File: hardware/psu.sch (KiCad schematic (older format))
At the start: 15 parts, among them U2 MIC5233-3.3

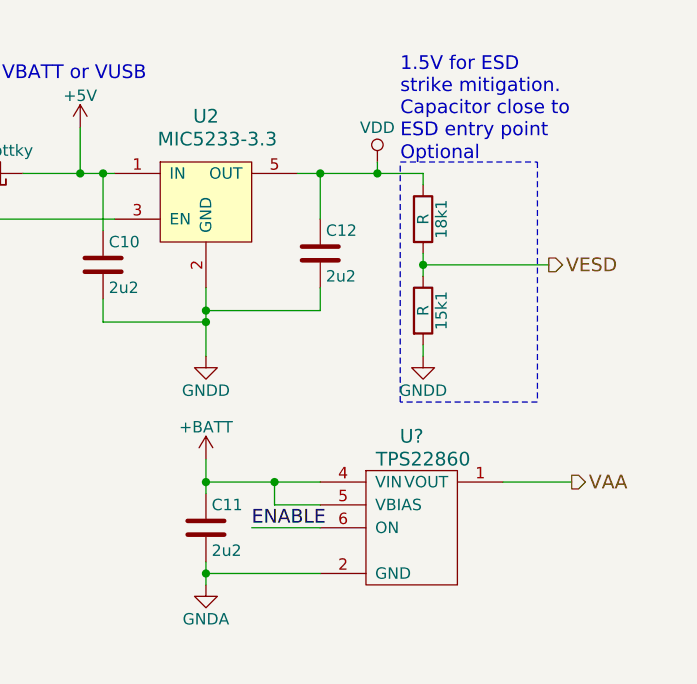
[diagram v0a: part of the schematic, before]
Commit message: Fix annotation of VESD resistors
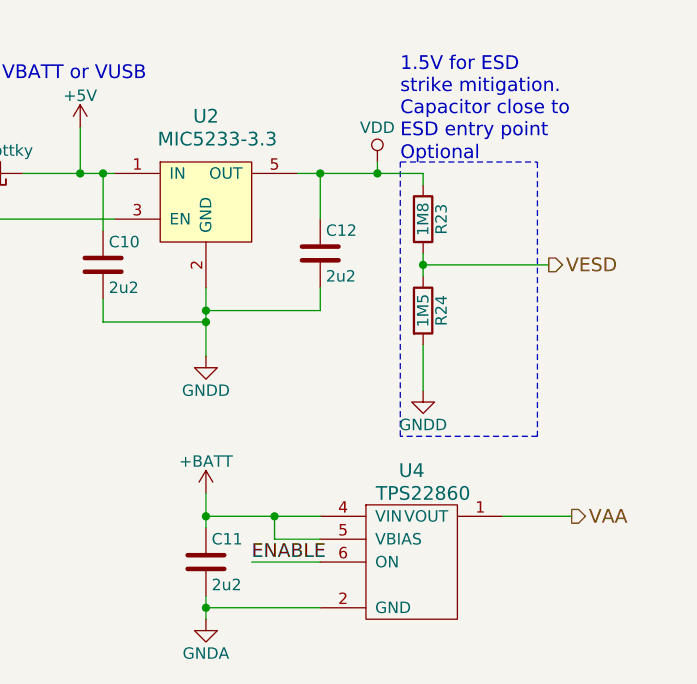
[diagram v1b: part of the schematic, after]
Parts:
- R23: renamed from 18k1; value R -> 1M8
- R24: renamed from 15k1; value R -> 1M5
- gave numbers to parts that had none: 1
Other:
- moved on the sheet: C11, U4
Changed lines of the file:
@@
 LIBS:mic5233-xx
 LIBS:bat54s
+LIBS:tps22860
 LIBS:musamasiina-cache
 EELAYER 25 0
@@
 $EndComp
 $Comp
-L GNDD #PWR025
+L GNDD #PWR27
 U 1 1 573FE50E
 P 3150 5550
-F 0 "#PWR025" H 3150 5300 50  0001 C CNN
+F 0 "#PWR27" H 3150 5300 50  0001 C CNN
 F 1 "GNDD" H 3150 5400 50  0000 C CNN
 F 2 "" H 3150 5550 50  0000 C CNN
@@
 $EndComp
 $Comp
-L +BATT #PWR026
+L +BATT #PWR25
 U 1 1 573FE50F
 P 1850 4550
-F 0 "#PWR026" H 1850 4400 50  0001 C CNN
+F 0 "#PWR25" H 1850 4400 50  0001 C CNN
 F 1 "+BATT" H 1850 4690 50  0000 C CNN
 F 2 "" H 1850 4550 50  0000 C CNN
@@
 $EndComp
 $Comp
-L VDD #PWR027
+L VDD #PWR33
 U 1 1 573FE51D
 P 3900 4700
-F 0 "#PWR027" H 3900 4550 50  0001 C CNN
+F 0 "#PWR33" H 3900 4550 50  0001 C CNN
 F 1 "VDD" H 3900 4850 50  0000 C CNN
 F 2 "" H 3900 4700 50  0000 C CNN
@@
 $EndComp
 $Comp
-L R 18k1
+L R R23
 U 1 1 573FE51E
 P 4100 4950
-F 0 "18k1" V 4180 4950 50  0000 C CNN
-F 1 "R" V 4100 4950 50  0000 C CNN
+F 0 "R23" V 4180 4950 50  0000 C CNN
+F 1 "1M8" V 4100 4950 50  0000 C CNN
 F 2 "" V 4030 4950 50  0000 C CNN
 F 3 "" H 4100 4950 50  0000 C CNN
@@
 $EndComp
 $Comp
-L R 15k1
+L R R24
 U 1 1 573FE51F
 P 4100 5350
-F 0 "15k1" V 4180 5350 50  0000 C CNN
-F 1 "R" V 4100 5350 50  0000 C CNN
+F 0 "R24" V 4180 5350 50  0000 C CNN
+F 1 "1M5" V 4100 5350 50  0000 C CNN
 F 2 "" V 4030 5350 50  0000 C CNN
 F 3 "" H 4100 5350 50  0000 C CNN
@@
 $EndComp
 $Comp
-L GNDD #PWR028
+L GNDD #PWR34
 U 1 1 573FE520
-P 4100 5550
-F 0 "#PWR028" H 4100 5300 50  0001 C CNN
-F 1 "GNDD" H 4100 5400 50  0000 C CNN
-F 2 "" H 4100 5550 50  0000 C CNN
-F 3 "" H 4100 5550 50  0000 C CNN
-	1    4100 5550
+P 4100 5700
+F 0 "#PWR34" H 4100 5450 50  0001 C CNN
+F 1 "GNDD" H 4100 5550 50  0000 C CNN
+F 2 "" H 4100 5700 50  0000 C CNN
+F 3 "" H 4100 5700 50  0000 C CNN
+	1    4100 5700
 	1    0    0    -1
 $EndComp
@@
 	4100 5100 4100 5200
 Wire Wire Line
-	4100 5500 4100 5550
+	4100 5500 4100 5700
 Wire Wire Line
 	4100 5150 4650 5150
@@
 	4000 4700 4600 4700
 Wire Notes Line
-	4600 4700 4600 5750
-Wire Notes Line
-	4600 5750 4000 5750
-Wire Notes Line
-	4000 5750 4000 4700
+	4600 4700 4600 5900
+Wire Notes Line
+	4600 5900 4000 5900
+Wire Notes Line
+	4000 5900 4000 4700
 Text Notes 4000 4700 0    60   ~ 0
 Optional
@@
 Powered by VBATT or VUSB
 $Comp
-L TPS22860 U?
+L TPS22860 U4
 U 1 1 573FE54A
-P 4050 6300
-F 0 "U?" H 4050 6700 60  0000 C CNN
-F 1 "TPS22860" H 4100 6600 60  0000 C CNN
-F 2 "" H 4050 6300 60  0000 C CNN
-F 3 "" H 4050 6300 60  0000 C CNN
-	1    4050 6300
-	1    0    0    -1
-$EndComp
-$Comp
-L +BATT #PWR029
+P 4050 6450
+F 0 "U4" H 4050 6850 60  0000 C CNN
+F 1 "TPS22860" H 4100 6750 60  0000 C CNN
+F 2 "" H 4050 6450 60  0000 C CNN
+F 3 "" H 4050 6450 60  0000 C CNN
+	1    4050 6450
+	1    0    0    -1
+$EndComp
+$Comp
+L +BATT #PWR28
 U 1 1 573FE54B
-P 3150 6000
-F 0 "#PWR029" H 3150 5850 50  0001 C CNN
-F 1 "+BATT" H 3150 6140 50  0000 C CNN
-F 2 "" H 3150 6000 50  0000 C CNN
-F 3 "" H 3150 6000 50  0000 C CNN
-	1    3150 6000
-	1    0    0    -1
-$EndComp
-Wire Wire Line
-	3150 6100 3650 6100
-Wire Wire Line
-	3450 6200 3650 6200
-Connection ~ 3450 6100
-Wire Wire Line
-	3350 6300 3650 6300
-Text Label 3350 6300 0    60   ~ 0
+P 3150 6150
+F 0 "#PWR28" H 3150 6000 50  0001 C CNN
+F 1 "+BATT" H 3150 6290 50  0000 C CNN
+F 2 "" H 3150 6150 50  0000 C CNN
+F 3 "" H 3150 6150 50  0000 C CNN
+	1    3150 6150
+	1    0    0    -1
+$EndComp
+Wire Wire Line
+	3150 6250 3650 6250
+Wire Wire Line
+	3450 6350 3650 6350
+Connection ~ 3450 6250
+Wire Wire Line
+	3350 6450 3650 6450
+Text Label 3350 6450 0    60   ~ 0
 ENABLE
 $Comp
-L GNDA #PWR030
+L GNDA #PWR29
 U 1 1 573FE54D
-P 3150 6550
-F 0 "#PWR030" H 3150 6300 50  0001 C CNN
-F 1 "GNDA" H 3150 6400 50  0000 C CNN
-F 2 "" H 3150 6550 50  0000 C CNN
-F 3 "" H 3150 6550 50  0000 C CNN
-	1    3150 6550
-	1    0    0    -1
-$EndComp
-Wire Wire Line
-	3150 6500 3650 6500
+P 3150 6700
+F 0 "#PWR29" H 3150 6450 50  0001 C CNN
+F 1 "GNDA" H 3150 6550 50  0000 C CNN
+F 2 "" H 3150 6700 50  0000 C CNN
+F 3 "" H 3150 6700 50  0000 C CNN
+	1    3150 6700
+	1    0    0    -1
+$EndComp
+Wire Wire Line
+	3150 6650 3650 6650
 $Comp
 L C C11
 U 1 1 573FE54E
-P 3150 6300
-F 0 "C11" H 3175 6400 50  0000 L CNN
-F 1 "2u2" H 3175 6200 50  0000 L CNN
-F 2 "" H 3188 6150 50  0000 C CNN
-F 3 "" H 3150 6300 50  0000 C CNN
-	1    3150 6300
-	1    0    0    -1
-$EndComp
-Wire Wire Line
-	3150 6000 3150 6150
-Connection ~ 3150 6100
-Wire Wire Line
-	3150 6450 3150 6550
-Connection ~ 3150 6500
-Wire Wire Line
-	3450 6200 3450 6100
-Wire Wire Line
-	4450 6100 4750 6100
+P 3150 6450
+F 0 "C11" H 3175 6550 50  0000 L CNN
+F 1 "2u2" H 3175 6350 50  0000 L CNN
+F 2 "" H 3188 6300 50  0000 C CNN
+F 3 "" H 3150 6450 50  0000 C CNN
+	1    3150 6450
+	1    0    0    -1
+$EndComp
+Wire Wire Line
+	3150 6150 3150 6300
+Connection ~ 3150 6250
+Wire Wire Line
+	3150 6600 3150 6700
+Connection ~ 3150 6650
+Wire Wire Line
+	3450 6350 3450 6250
+Wire Wire Line
+	4450 6250 4750 6250
 Text HLabel 2200 1550 0    60   Input ~ 0
 VBUS
@@
 	3700 1450 4850 1450
 $Comp
-L GNDD #PWR031
+L GNDD #PWR32
 U 1 1 57401DD2
 P 3700 2650
-F 0 "#PWR031" H 3700 2400 50  0001 C CNN
+F 0 "#PWR32" H 3700 2400 50  0001 C CNN
 F 1 "GNDD" H 3700 2500 50  0000 C CNN
 F 2 "" H 3700 2650 50  0000 C CNN
@@
 $EndComp
 $Comp
-L +5V #PWR032
+L +5V #PWR31
 U 1 1 57402100
 P 3700 1400
-F 0 "#PWR032" H 3700 1250 50  0001 C CNN
+F 0 "#PWR31" H 3700 1250 50  0001 C CNN
 F 1 "+5V" H 3700 1540 50  0000 C CNN
 F 2 "" H 3700 1400 50  0000 C CNN
@@
 $EndComp
 $Comp
-L +5V #PWR033
+L +5V #PWR26
 U 1 1 57402256
 P 2600 4550
-F 0 "#PWR033" H 2600 4400 50  0001 C CNN
+F 0 "#PWR26" H 2600 4400 50  0001 C CNN
 F 1 "+5V" H 2600 4690 50  0000 C CNN
 F 2 "" H 2600 4550 50  0000 C CNN
@@
 Text HLabel 2150 4950 0    60   Input ~ 0
 ENABLE
-Text HLabel 4750 6100 2    60   Output ~ 0
+Text HLabel 4750 6250 2    60   Output ~ 0
 VAA
 Text HLabel 4850 1450 2    60   Output ~ 0
@@
 	3250 3450 3250 3550
 $Comp
-L GNDD #PWR034
+L GNDD #PWR30
 U 1 1 57407F45
 P 3250 3550
-F 0 "#PWR034" H 3250 3300 50  0001 C CNN
+F 0 "#PWR30" H 3250 3300 50  0001 C CNN
 F 1 "GNDD" H 3250 3400 50  0000 C CNN
 F 2 "" H 3250 3550 50  0000 C CNN

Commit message: Start placement of parts
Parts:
- C10, C11, C12, C13: footprint (none) -> footprints:SMD0805-CAP-M
- D4, D5: footprint (none) -> footprints:SOD323-M
- D6: footprint (none) -> footprints:SMD0805-LED-M
- FB1, FB2: footprint (none) -> footprints:SMD0805-FERRITE-M
- R23, R24, R8: footprint (none) -> footprints:SMD0805-RES-M
- U2: footprint (none) -> footprints:SOT23-6-M
- U4: footprint (none) -> footprints:SOT23-5-M
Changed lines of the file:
@@
 F 0 "FB1" H 2800 1700 50  0000 C CNN
 F 1 "FILTER" H 2800 1450 50  0000 C CNN
-F 2 "" H 2800 1550 50  0000 C CNN
+F 2 "footprints:SMD0805-FERRITE-M" H 2800 1550 50  0001 C CNN
 F 3 "" H 2800 1550 50  0000 C CNN
 	1    2800 1550
@@
 F 0 "FB2" H 2800 2100 50  0000 C CNN
 F 1 "FILTER" H 2800 1850 50  0000 C CNN
-F 2 "" H 2800 1950 50  0000 C CNN
+F 2 "footprints:SMD0805-FERRITE-M" H 2800 1950 50  0001 C CNN
 F 3 "" H 2800 1950 50  0000 C CNN
 	1    2800 1950
@@
 F 0 "C13" H 3725 1850 50  0000 L CNN
 F 1 "2u2" H 3725 1650 50  0000 L CNN
-F 2 "" H 3738 1600 50  0000 C CNN
+F 2 "footprints:SMD0805-CAP-M" H 3738 1600 50  0001 C CNN
 F 3 "" H 3700 1750 50  0000 C CNN
 	1    3700 1750
@@
 F 0 "D5" H 3250 1850 50  0000 C CNN
 F 1 "ZENER" H 3250 1650 50  0000 C CNN
-F 2 "" H 3250 1750 50  0000 C CNN
+F 2 "footprints:SOD323-M" H 3250 1750 50  0001 C CNN
 F 3 "" H 3250 1750 50  0000 C CNN
 	1    3250 1750
@@
 F 0 "U2" H 3150 5200 60  0000 C CNN
 F 1 "MIC5233-3.3" H 3200 5100 60  0000 C CNN
-F 2 "" H 3150 4850 60  0000 C CNN
+F 2 "footprints:SOT23-6-M" H 3150 4850 60  0001 C CNN
 F 3 "" H 3150 4850 60  0000 C CNN
 	1    3150 4850
@@
 $EndComp
 $Comp
-L GNDD #PWR27
+L GNDD #PWR025
 U 1 1 573FE50E
 P 3150 5550
-F 0 "#PWR27" H 3150 5300 50  0001 C CNN
+F 0 "#PWR025" H 3150 5300 50  0001 C CNN
 F 1 "GNDD" H 3150 5400 50  0000 C CNN
 F 2 "" H 3150 5550 50  0000 C CNN
@@
 $EndComp
 $Comp
-L +BATT #PWR25
+L +BATT #PWR026
 U 1 1 573FE50F
 P 1850 4550
-F 0 "#PWR25" H 1850 4400 50  0001 C CNN
+F 0 "#PWR026" H 1850 4400 50  0001 C CNN
 F 1 "+BATT" H 1850 4690 50  0000 C CNN
 F 2 "" H 1850 4550 50  0000 C CNN
@@
 F 0 "D6" H 4300 2250 50  0000 C CNN
 F 1 "LED" H 4300 2050 50  0000 C CNN
-F 2 "" H 4300 2150 50  0000 C CNN
+F 2 "footprints:SMD0805-LED-M" H 4300 2150 50  0001 C CNN
 F 3 "" H 4300 2150 50  0000 C CNN
 	1    4300 2150
@@
 F 0 "C10" H 2725 5250 50  0000 L CNN
 F 1 "2u2" H 2725 5050 50  0000 L CNN
-F 2 "" H 2738 5000 50  0000 C CNN
+F 2 "footprints:SMD0805-CAP-M" H 2738 5000 50  0001 C CNN
 F 3 "" H 2700 5150 50  0000 C CNN
 	1    2700 5150
@@
 F 0 "C12" H 3675 5200 50  0000 L CNN
 F 1 "2u2" H 3675 5000 50  0000 L CNN
-F 2 "" H 3688 4950 50  0000 C CNN
+F 2 "footprints:SMD0805-CAP-M" H 3688 4950 50  0001 C CNN
 F 3 "" H 3650 5100 50  0000 C CNN
 	1    3650 5100
@@
 F 0 "R8" V 4380 1750 50  0000 C CNN
 F 1 "10k" V 4300 1750 50  0000 C CNN
-F 2 "" V 4230 1750 50  0000 C CNN
+F 2 "footprints:SMD0805-RES-M" V 4230 1750 50  0001 C CNN
 F 3 "" H 4300 1750 50  0000 C CNN
 	1    4300 1750
@@
 $EndComp
 $Comp
-L VDD #PWR33
+L VDD #PWR027
 U 1 1 573FE51D
 P 3900 4700
-F 0 "#PWR33" H 3900 4550 50  0001 C CNN
+F 0 "#PWR027" H 3900 4550 50  0001 C CNN
 F 1 "VDD" H 3900 4850 50  0000 C CNN
 F 2 "" H 3900 4700 50  0000 C CNN
@@
 F 0 "R23" V 4180 4950 50  0000 C CNN
 F 1 "1M8" V 4100 4950 50  0000 C CNN
-F 2 "" V 4030 4950 50  0000 C CNN
+F 2 "footprints:SMD0805-RES-M" V 4030 4950 50  0001 C CNN
 F 3 "" H 4100 4950 50  0000 C CNN
 	1    4100 4950
@@
 F 0 "R24" V 4180 5350 50  0000 C CNN
 F 1 "1M5" V 4100 5350 50  0000 C CNN
-F 2 "" V 4030 5350 50  0000 C CNN
+F 2 "footprints:SMD0805-RES-M" V 4030 5350 50  0001 C CNN
 F 3 "" H 4100 5350 50  0000 C CNN
 	1    4100 5350
@@
 $EndComp
 $Comp
-L GNDD #PWR34
+L GNDD #PWR028
 U 1 1 573FE520
 P 4100 5700
-F 0 "#PWR34" H 4100 5450 50  0001 C CNN
+F 0 "#PWR028" H 4100 5450 50  0001 C CNN
 F 1 "GNDD" H 4100 5550 50  0000 C CNN
 F 2 "" H 4100 5700 50  0000 C CNN
@@
 F 0 "D4" H 2200 4850 50  0000 C CNN
 F 1 "D_Schottky" H 2200 4650 50  0000 C CNN
-F 2 "" H 2200 4750 50  0000 C CNN
+F 2 "footprints:SOD323-M" H 2200 4750 50  0001 C CNN
 F 3 "" H 2200 4750 50  0000 C CNN
 	1    2200 4750
@@
 F 0 "U4" H 4050 6850 60  0000 C CNN
 F 1 "TPS22860" H 4100 6750 60  0000 C CNN
-F 2 "" H 4050 6450 60  0000 C CNN
+F 2 "footprints:SOT23-5-M" H 4050 6450 60  0001 C CNN
 F 3 "" H 4050 6450 60  0000 C CNN
 	1    4050 6450
@@
 $EndComp
 $Comp
-L +BATT #PWR28
+L +BATT #PWR029
 U 1 1 573FE54B
 P 3150 6150
-F 0 "#PWR28" H 3150 6000 50  0001 C CNN
+F 0 "#PWR029" H 3150 6000 50  0001 C CNN
 F 1 "+BATT" H 3150 6290 50  0000 C CNN
 F 2 "" H 3150 6150 50  0000 C CNN
@@
 ENABLE
 $Comp
-L GNDA #PWR29
+L GNDA #PWR030
 U 1 1 573FE54D
 P 3150 6700
-F 0 "#PWR29" H 3150 6450 50  0001 C CNN
+F 0 "#PWR030" H 3150 6450 50  0001 C CNN
 F 1 "GNDA" H 3150 6550 50  0000 C CNN
 F 2 "" H 3150 6700 50  0000 C CNN
@@
 F 0 "C11" H 3175 6550 50  0000 L CNN
 F 1 "2u2" H 3175 6350 50  0000 L CNN
-F 2 "" H 3188 6300 50  0000 C CNN
+F 2 "footprints:SMD0805-CAP-M" H 3188 6300 50  0001 C CNN
 F 3 "" H 3150 6450 50  0000 C CNN
 	1    3150 6450
@@
 	3700 1450 4850 1450
 $Comp
-L GNDD #PWR32
+L GNDD #PWR031
 U 1 1 57401DD2
 P 3700 2650
-F 0 "#PWR32" H 3700 2400 50  0001 C CNN
+F 0 "#PWR031" H 3700 2400 50  0001 C CNN
 F 1 "GNDD" H 3700 2500 50  0000 C CNN
 F 2 "" H 3700 2650 50  0000 C CNN
@@
 $EndComp
 $Comp
-L +5V #PWR31
+L +5V #PWR032
 U 1 1 57402100
 P 3700 1400
-F 0 "#PWR31" H 3700 1250 50  0001 C CNN
+F 0 "#PWR032" H 3700 1250 50  0001 C CNN
 F 1 "+5V" H 3700 1540 50  0000 C CNN
 F 2 "" H 3700 1400 50  0000 C CNN
@@
 $EndComp
 $Comp
-L +5V #PWR26
+L +5V #PWR033
 U 1 1 57402256
 P 2600 4550
-F 0 "#PWR26" H 2600 4400 50  0001 C CNN
+F 0 "#PWR033" H 2600 4400 50  0001 C CNN
 F 1 "+5V" H 2600 4690 50  0000 C CNN
 F 2 "" H 2600 4550 50  0000 C CNN
@@
 F 0 "BT1" H 3350 3350 50  0000 L CNN
 F 1 "Battery" H 3350 3250 50  0000 L CNN
-F 2 "" V 3250 3340 50  0000 C CNN
+F 2 "" V 3250 3340 50  0001 C CNN
 F 3 "" V 3250 3340 50  0000 C CNN
 	1    3250 3300
@@
 	3250 3450 3250 3550
 $Comp
-L GNDD #PWR30
+L GNDD #PWR034
 U 1 1 57407F45
 P 3250 3550
-F 0 "#PWR30" H 3250 3300 50  0001 C CNN
+F 0 "#PWR034" H 3250 3300 50  0001 C CNN
 F 1 "GNDD" H 3250 3400 50  0000 C CNN
 F 2 "" H 3250 3550 50  0000 C CNN

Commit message: Update schematics
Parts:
- added C28: 2u2, footprints:SMD0805-CAP-M, symbol C
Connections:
- net GNDA: now also C28.2; no longer C11.2
- net GNDD: now also C11.2
- net VAA: now also C28.1
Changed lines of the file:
@@
 $EndComp
 $Comp
-L GNDD #PWR028
+L GNDD #PWR30
 U 1 1 573FE50E
 P 3150 5550
-F 0 "#PWR028" H 3150 5300 50  0001 C CNN
+F 0 "#PWR30" H 3150 5300 50  0001 C CNN
 F 1 "GNDD" H 3150 5400 50  0000 C CNN
 F 2 "" H 3150 5550 50  0000 C CNN
@@
 $EndComp
 $Comp
-L +BATT #PWR029
+L +BATT #PWR28
 U 1 1 573FE50F
 P 1850 4550
-F 0 "#PWR029" H 1850 4400 50  0001 C CNN
+F 0 "#PWR28" H 1850 4400 50  0001 C CNN
 F 1 "+BATT" H 1850 4690 50  0000 C CNN
 F 2 "" H 1850 4550 50  0000 C CNN
@@
 $EndComp
 $Comp
-L VDD #PWR030
+L VDD #PWR37
 U 1 1 573FE51D
 P 3900 4700
-F 0 "#PWR030" H 3900 4550 50  0001 C CNN
+F 0 "#PWR37" H 3900 4550 50  0001 C CNN
 F 1 "VDD" H 3900 4850 50  0000 C CNN
 F 2 "" H 3900 4700 50  0000 C CNN
@@
 $EndComp
 $Comp
-L GNDD #PWR031
+L GNDD #PWR38
 U 1 1 573FE520
 P 4100 5700
-F 0 "#PWR031" H 4100 5450 50  0001 C CNN
+F 0 "#PWR38" H 4100 5450 50  0001 C CNN
 F 1 "GNDD" H 4100 5550 50  0000 C CNN
 F 2 "" H 4100 5700 50  0000 C CNN
@@
 $EndComp
 $Comp
-L +BATT #PWR032
+L +BATT #PWR31
 U 1 1 573FE54B
 P 3150 6150
-F 0 "#PWR032" H 3150 6000 50  0001 C CNN
+F 0 "#PWR31" H 3150 6000 50  0001 C CNN
 F 1 "+BATT" H 3150 6290 50  0000 C CNN
 F 2 "" H 3150 6150 50  0000 C CNN
@@
 Text Label 3350 6450 0    60   ~ 0
 ENABLE
-$Comp
-L GNDA #PWR033
-U 1 1 573FE54D
-P 3150 6700
-F 0 "#PWR033" H 3150 6450 50  0001 C CNN
-F 1 "GNDA" H 3150 6550 50  0000 C CNN
-F 2 "" H 3150 6700 50  0000 C CNN
-F 3 "" H 3150 6700 50  0000 C CNN
-	1    3150 6700
-	1    0    0    -1
-$EndComp
-Wire Wire Line
-	3150 6650 3650 6650
 $Comp
 L C C11
@@
 Wire Wire Line
 	3150 6600 3150 6700
-Connection ~ 3150 6650
 Wire Wire Line
 	3450 6350 3450 6250
@@
 	3700 1450 4850 1450
 $Comp
-L GNDD #PWR034
+L GNDD #PWR36
 U 1 1 57401DD2
 P 3700 2650
-F 0 "#PWR034" H 3700 2400 50  0001 C CNN
+F 0 "#PWR36" H 3700 2400 50  0001 C CNN
 F 1 "GNDD" H 3700 2500 50  0000 C CNN
 F 2 "" H 3700 2650 50  0000 C CNN
@@
 $EndComp
 $Comp
-L +5V #PWR035
+L +5V #PWR35
 U 1 1 57402100
 P 3700 1400
-F 0 "#PWR035" H 3700 1250 50  0001 C CNN
+F 0 "#PWR35" H 3700 1250 50  0001 C CNN
 F 1 "+5V" H 3700 1540 50  0000 C CNN
 F 2 "" H 3700 1400 50  0000 C CNN
@@
 $EndComp
 $Comp
-L +5V #PWR036
+L +5V #PWR29
 U 1 1 57402256
 P 2600 4550
-F 0 "#PWR036" H 2600 4400 50  0001 C CNN
+F 0 "#PWR29" H 2600 4400 50  0001 C CNN
 F 1 "+5V" H 2600 4690 50  0000 C CNN
 F 2 "" H 2600 4550 50  0000 C CNN
@@
 	3250 3450 3250 3550
 $Comp
-L GNDD #PWR037
+L GNDD #PWR33
 U 1 1 57407F45
 P 3250 3550
-F 0 "#PWR037" H 3250 3300 50  0001 C CNN
+F 0 "#PWR33" H 3250 3300 50  0001 C CNN
 F 1 "GNDD" H 3250 3400 50  0000 C CNN
 F 2 "" H 3250 3550 50  0000 C CNN
@@
 	1    0    0    -1
 $EndComp
+$Comp
+L GNDD #PWR32
+U 1 1 574AF4C9
+P 3150 6700
+F 0 "#PWR32" H 3150 6450 50  0001 C CNN
+F 1 "GNDD" H 3150 6550 50  0000 C CNN
+F 2 "" H 3150 6700 50  0000 C CNN
+F 3 "" H 3150 6700 50  0000 C CNN
+	1    3150 6700
+	1    0    0    -1
+$EndComp
+$Comp
+L C C28
+U 1 1 574AF501
+P 4550 6500
+F 0 "C28" H 4575 6600 50  0000 L CNN
+F 1 "2u2" H 4575 6400 50  0000 L CNN
+F 2 "footprints:SMD0805-CAP-M" H 4588 6350 50  0001 C CNN
+F 3 "" H 4550 6500 50  0000 C CNN
+	1    4550 6500
+	1    0    0    -1
+$EndComp
+Wire Wire Line
+	3650 6650 3550 6650
+Wire Wire Line
+	3550 6650 3550 6700
+Wire Wire Line
+	4550 6350 4550 6250
+Connection ~ 4550 6250
+Wire Wire Line
+	4550 6650 4550 6700
+$Comp
+L GNDA #PWR39
+U 1 1 574AF85C
+P 4550 6700
+F 0 "#PWR39" H 4550 6450 50  0001 C CNN
+F 1 "GNDA" H 4550 6550 50  0000 C CNN
+F 2 "" H 4550 6700 50  0000 C CNN
+F 3 "" H 4550 6700 50  0000 C CNN
+	1    4550 6700
+	1    0    0    -1
+$EndComp
+$Comp
+L GNDA #PWR34
+U 1 1 574AFAC0
+P 3550 6700
+F 0 "#PWR34" H 3550 6450 50  0001 C CNN
+F 1 "GNDA" H 3550 6550 50  0000 C CNN
+F 2 "" H 3550 6700 50  0000 C CNN
+F 3 "" H 3550 6700 50  0000 C CNN
+	1    3550 6700
+	1    0    0    -1
+$EndComp
